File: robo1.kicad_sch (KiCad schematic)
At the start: 28 parts, among them J1 Conn_02x05_Odd_Even, J2 Conn_02x05_Odd_Even, J3 Conn_01x04_Pin, J4 Conn_01x04_Pin, J5 Screw_Terminal_01x02, J6 Screw_Terminal_01x02, J7 Conn_01x03_Pin, J8 Conn_01x03_Pin, SW1 SW_Push, SW2 SW_Push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

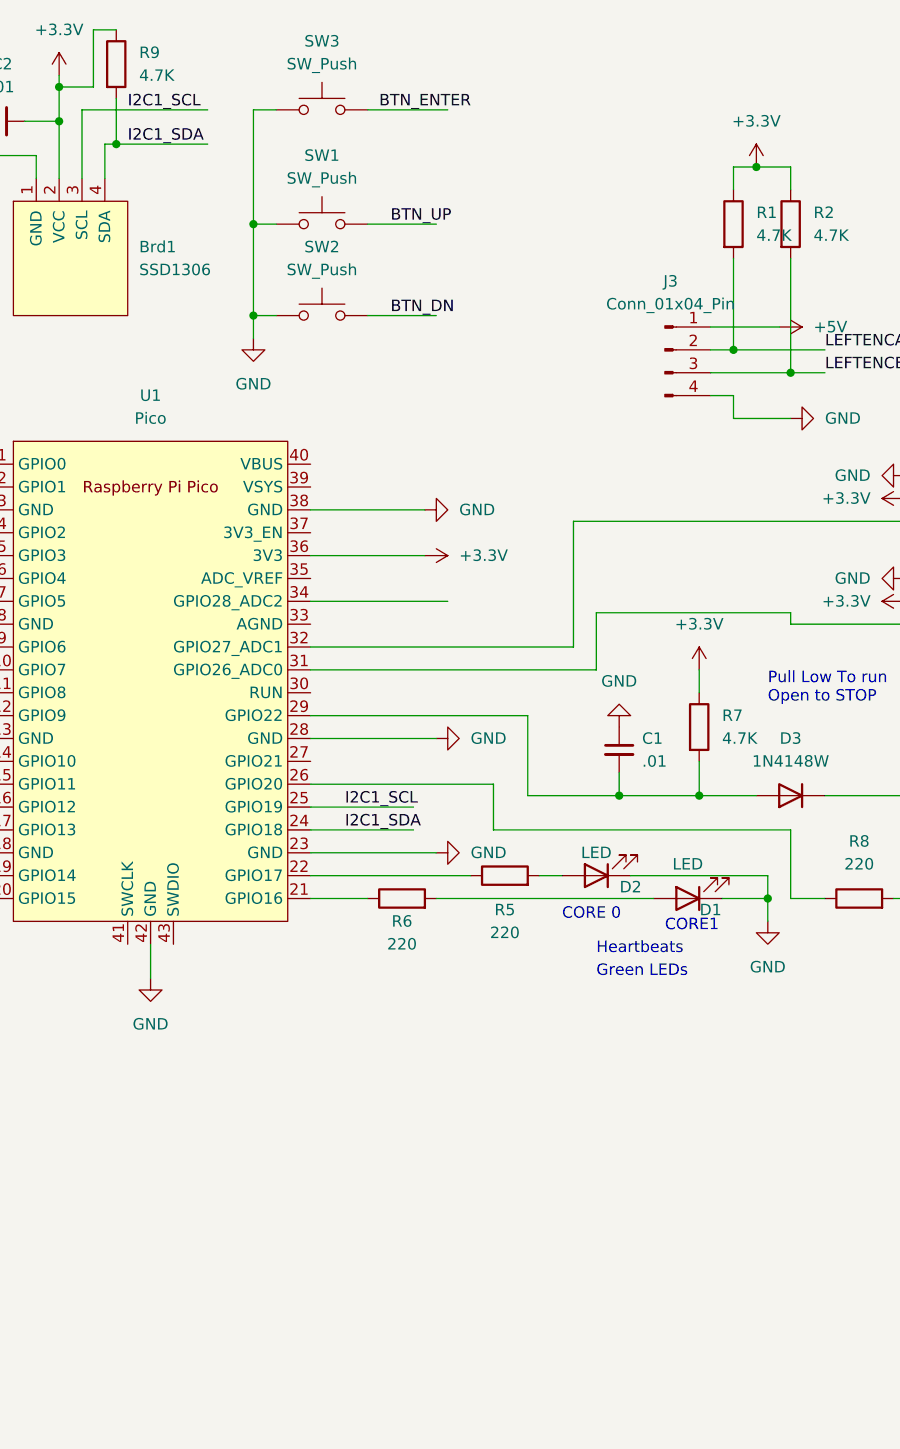
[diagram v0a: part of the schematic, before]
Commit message: update to use ad5590 and pb encoder
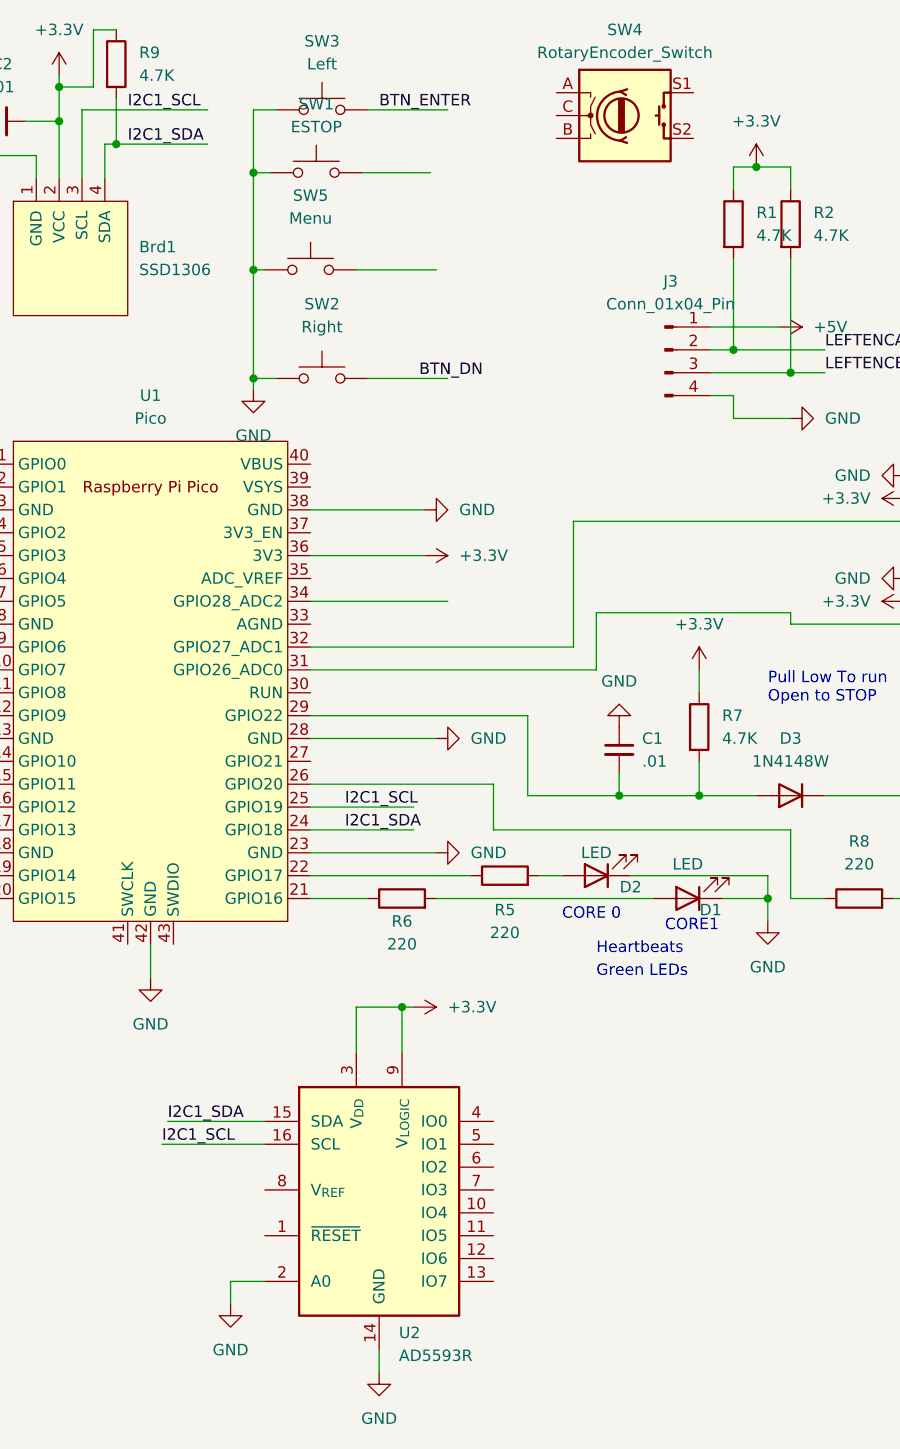
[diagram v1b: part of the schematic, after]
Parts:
- added SW4: RotaryEncoder_Switch, Rotary_Encoder:RotaryEncoder_Alps_EC11E-Switch_Vertical_H20mm_CircularMountingHoles, symbol Device:RotaryEncoder_Switch
- added SW5: Menu, Button_Switch_THT:SW_PUSH_6mm, symbol Switch:SW_Push
- added U2: AD5593R, Package_SO:TSSOP-16_4.4x5mm_P0.65mm, symbol Analog:AD5593R
- SW1: value SW_Push -> ESTOP
- SW2: value SW_Push -> Right
- SW3: value SW_Push -> Left
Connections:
- net +3.3V: now also U2.3 (V_{DD}), U2.9 (V_{LOGIC})
- net GND: now also SW5.1, U2.14 (GND), U2.2 (A0)
- net I2C1_SCL: now also U2.16 (SCL)
- net I2C1_SDA: now also U2.15 (SDA)
- net BTN_UP: no longer names the net of SW1.2
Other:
- moved on the sheet: SW1, SW2

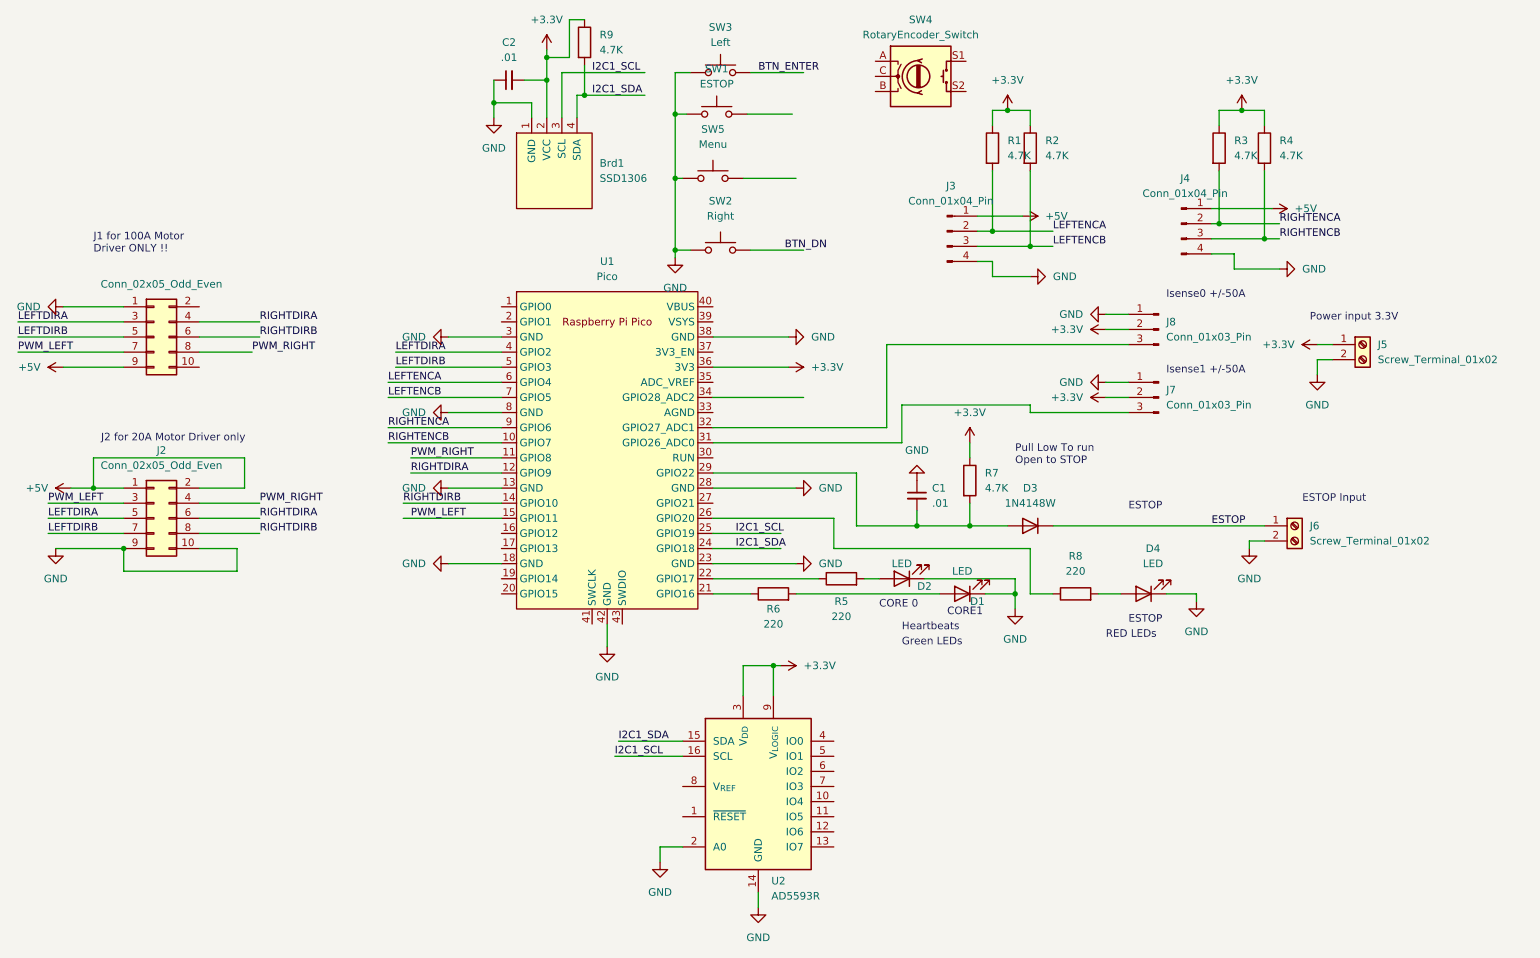
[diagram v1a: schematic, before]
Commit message: add 5593 gpio
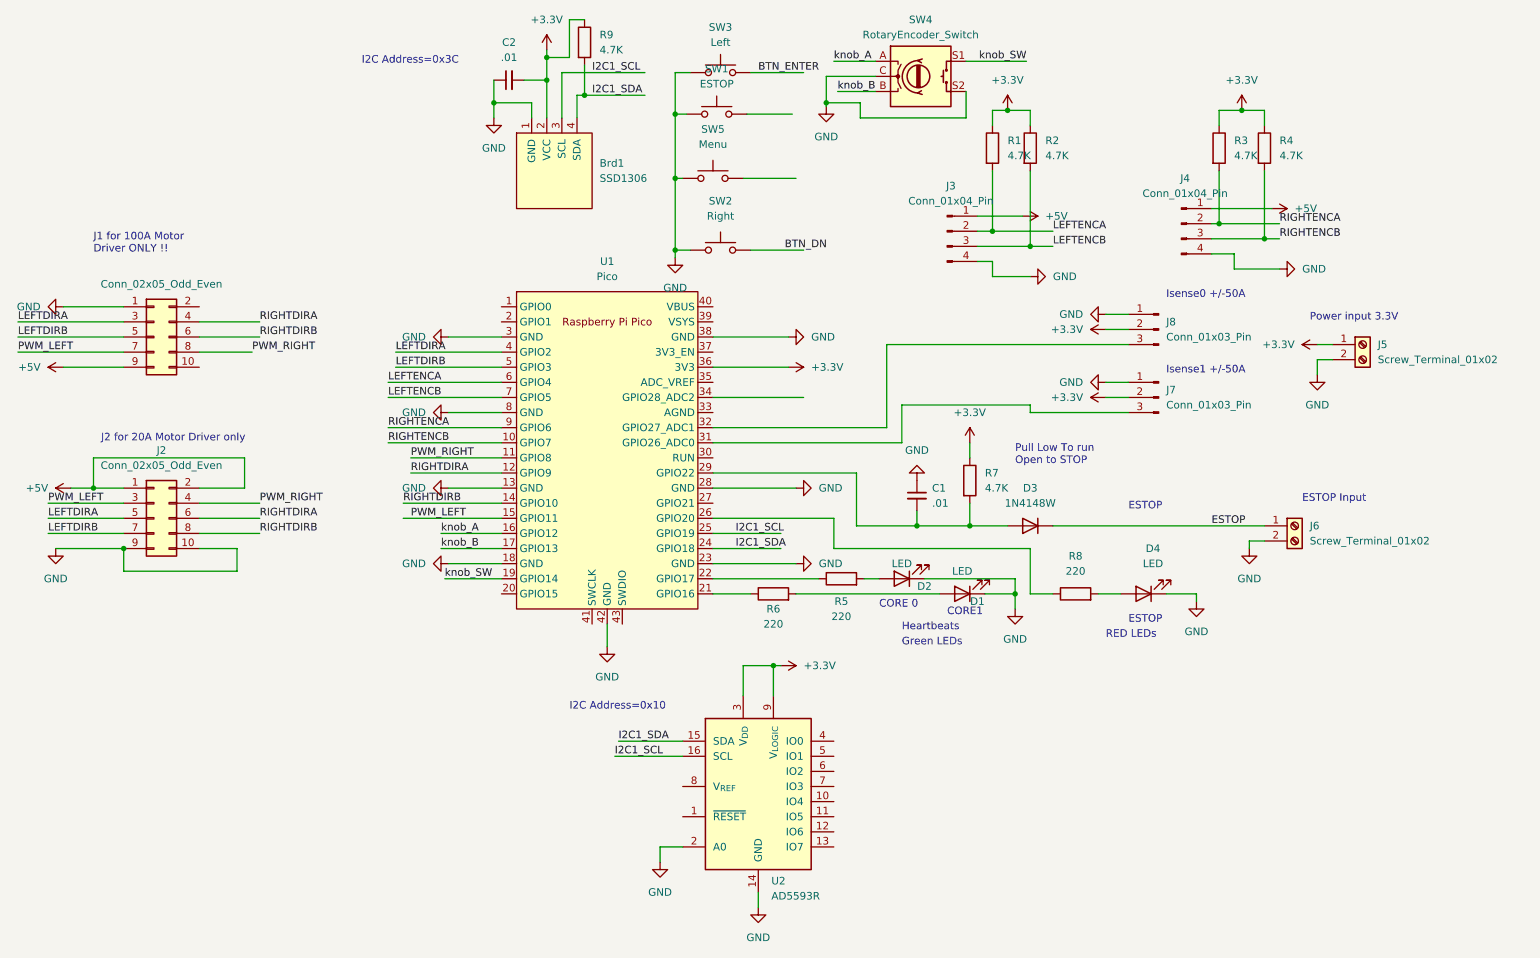
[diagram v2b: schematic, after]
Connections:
- net GND: now also SW4.C, SW4.S2
- net knob_A: now reaches SW4.A
- net knob_A: now also U1.16 (GPIO12)
- net knob_B: now reaches SW4.B
- net knob_B: now also U1.17 (GPIO13)
- net knob_SW: now reaches SW4.S1
- net knob_SW: now also U1.19 (GPIO14)
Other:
- note added: "I2C Address=0x10"
- note added: "I2C Address=0x3C"
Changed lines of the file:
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@@
   (junction (at 213.36 49.53) (diameter 0) (color 0 0 0 0)
   )
+  (junction (at 185.42 27.94) (diameter 0) (color 0 0 0 0)
+  )
   (junction (at 160.02 29.845) (diameter 0) (color 0 0 0 0)
   )
@@
     (stroke (width 0) (type default))
   )
+  (wire (pts (xy 193.675 23.495) (xy 185.42 23.495))
+    (stroke (width 0) (type default))
+  )
   (wire (pts (xy 217.17 107.95) (xy 217.17 110.49))
     (stroke (width 0) (type default))
@@
     (stroke (width 0) (type default))
   )
+  (wire (pts (xy 208.915 30.48) (xy 208.915 26.035))
+    (stroke (width 0) (type default))
+  )
   (wire (pts (xy 219.71 78.74) (xy 219.71 80.01))
     (stroke (width 0) (type default))
@@
     (stroke (width 0) (type default))
   )
+  (wire (pts (xy 130.81 102.87) (xy 120.65 102.87))
+    (stroke (width 0) (type default))
+  )
   (wire (pts (xy 173.99 160.655) (xy 173.99 163.195))
     (stroke (width 0) (type default))
@@
     (stroke (width 0) (type default))
   )
+  (wire (pts (xy 191.135 30.48) (xy 208.915 30.48))
+    (stroke (width 0) (type default))
+  )
   (wire (pts (xy 198.12 85.09) (xy 198.12 78.74))
     (stroke (width 0) (type default))
@@
     (stroke (width 0) (type default))
   )
+  (wire (pts (xy 185.42 27.94) (xy 191.135 27.94))
+    (stroke (width 0) (type default))
+  )
   (wire (pts (xy 195.58 68.58) (xy 195.58 82.55))
     (stroke (width 0) (type default))
   )
+  (wire (pts (xy 130.81 100.33) (xy 120.65 100.33))
+    (stroke (width 0) (type default))
+  )
   (wire (pts (xy 55.88 102.87) (xy 67.31 102.87))
     (stroke (width 0) (type default))
@@
     (stroke (width 0) (type default))
   )
+  (wire (pts (xy 193.675 20.955) (xy 186.69 20.955))
+    (stroke (width 0) (type default))
+  )
   (wire (pts (xy 115.57 90.17) (xy 130.81 90.17))
     (stroke (width 0) (type default))
@@
     (stroke (width 0) (type default))
   )
+  (wire (pts (xy 219.075 20.955) (xy 208.915 20.955))
+    (stroke (width 0) (type default))
+  )
   (wire (pts (xy 166.37 82.55) (xy 195.58 82.55))
     (stroke (width 0) (type default))
@@
     (stroke (width 0) (type default))
   )
+  (wire (pts (xy 185.42 27.94) (xy 185.42 28.575))
+    (stroke (width 0) (type default))
+  )
   (wire (pts (xy 54.61 95.25) (xy 67.31 95.25))
     (stroke (width 0) (type default))
@@
     (stroke (width 0) (type default))
   )
+  (wire (pts (xy 130.81 107.95) (xy 121.285 107.95))
+    (stroke (width 0) (type default))
+  )
   (wire (pts (xy 150.495 135.255) (xy 161.29 135.255))
     (stroke (width 0) (type default))
@@
     (stroke (width 0) (type default))
   )
+  (wire (pts (xy 191.135 27.94) (xy 191.135 30.48))
+    (stroke (width 0) (type default))
+  )
   (wire (pts (xy 144.78 21.59) (xy 144.78 26.67))
     (stroke (width 0) (type default))
@@
     (stroke (width 0) (type default))
   )
+  (wire (pts (xy 185.42 23.495) (xy 185.42 27.94))
+    (stroke (width 0) (type default))
+  )
   (wire (pts (xy 54.61 100.33) (xy 67.31 100.33))
     (stroke (width 0) (type default))
@@
     (stroke (width 0) (type default))
   )
+  (wire (pts (xy 193.675 26.035) (xy 187.325 26.035))
+    (stroke (width 0) (type default))
+  )
   (text "ESTOP Input" (at 265.43 95.25 0)
     (effects (font (size 1.27 1.27)) (justify left bottom))
@@
     (effects (font (size 1.27 1.27)) (justify left bottom))
   )
+  (text "I2C Address=0x3C\n" (at 107.315 21.59 0)
+    (effects (font (size 1.27 1.27)) (justify left bottom))
+  )
   (text "CORE1" (at 205.74 114.3 0)
     (effects (font (size 1.27 1.27)) (justify left bottom))
@@
     (effects (font (size 1.27 1.27)) (justify left bottom))
   )
+  (text "I2C Address=0x10" (at 142.24 130.175 0)
+    (effects (font (size 1.27 1.27)) (justify left bottom))
+  )
   (label "RIGHTDIRA" (at 115.57 90.17 0) (fields_autoplaced)
     (effects (font (size 1.27 1.27)) (justify left bottom))
@@
     (effects (font (size 1.27 1.27)) (justify left bottom))
   )
+  (label "knob_A" (at 120.65 100.33 0) (fields_autoplaced)
+    (effects (font (size 1.27 1.27)) (justify left bottom))
+  )
   (label "I2C1_SDA" (at 170.18 102.87 0) (fields_autoplaced)
     (effects (font (size 1.27 1.27)) (justify left bottom))
@@
     (effects (font (size 1.27 1.27)) (justify left bottom))
   )
+  (label "knob_SW" (at 121.285 107.95 0) (fields_autoplaced)
+    (effects (font (size 1.27 1.27)) (justify left bottom))
+  )
+  (label "knob_SW" (at 219.075 20.955 180) (fields_autoplaced)
+    (effects (font (size 1.27 1.27)) (justify right bottom))
+  )
   (label "PWM_LEFT" (at 49.53 69.85 0) (fields_autoplaced)
     (effects (font (size 1.27 1.27)) (justify left bottom))
@@
     (effects (font (size 1.27 1.27)) (justify left bottom))
   )
+  (label "knob_B" (at 120.65 102.87 0) (fields_autoplaced)
+    (effects (font (size 1.27 1.27)) (justify left bottom))
+  )
   (label "I2C1_SCL" (at 149.86 137.795 0) (fields_autoplaced)
     (effects (font (size 1.27 1.27)) (justify left bottom))
@@
     (effects (font (size 1.27 1.27)) (justify left bottom))
   )
+  (label "knob_A" (at 186.69 20.955 0) (fields_autoplaced)
+    (effects (font (size 1.27 1.27)) (justify left bottom))
+  )
   (label "PWM_LEFT" (at 54.61 95.25 0) (fields_autoplaced)
     (effects (font (size 1.27 1.27)) (justify left bottom))
@@
   )
   (label "LEFTDIRB" (at 49.53 67.31 0) (fields_autoplaced)
+    (effects (font (size 1.27 1.27)) (justify left bottom))
+  )
+  (label "knob_B" (at 187.325 26.035 0) (fields_autoplaced)
     (effects (font (size 1.27 1.27)) (justify left bottom))
   )
@@
         )
       )
+    )
+  )
+  (symbol (lib_id "power:GND") (at 185.42 28.575 0) (unit 1)
+    (in_bom yes) (on_board yes) (dnp no) (fields_autoplaced)
+    (property "Reference" "#PWR037" (at 185.42 34.925 0)
+      (effects (font (size 1.27 1.27)) hide)
+    )
+    (property "Value" "GND" (at 185.42 33.655 0)
+      (effects (font (size 1.27 1.27)))
+    )
+    (property "Footprint" "" (at 185.42 28.575 0)
+      (effects (font (size 1.27 1.27)) hide)
+    )
+    (property "Datasheet" "" (at 185.42 28.575 0)
+      (effects (font (size 1.27 1.27)) hide)
+    )
+    (pin "1")
+    (instances
+      (project "robo1"
+        (path "/630901c0-a052-4661-a40a-8cd70c2ee20e"
+          (reference "#PWR037") (unit 1)
+        )
+      )
